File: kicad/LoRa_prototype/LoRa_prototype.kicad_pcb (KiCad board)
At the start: 4 copper layers, 138 parts, among them J1 Conn_ST_STDC14, J10 SYS, J11 BME, J12 GPS, J13 GPS_UART, J14 SPI_FLASH, J15 SYS, J18 MCO, J2 USB_C_Receptacle_PowerOnly_6P, J3 BAT, J4 SMA Female, J5 FG, J6 I2C1, J8 BMV, J9 UART1, Q1 DTC143Z, Q2 DTC143Z, SW1 NRST, U1 TC1262-33, U10 STM32WL54CCUx, U2 BQ24074RGTT, U3 MAX17048, U4 SPV1050, U5 AS179-92LF, U6 L80-R, U7 BME688, U8 W25Q16JVSS, U9 BMV080, X1 LSE, X2 NT2016SF

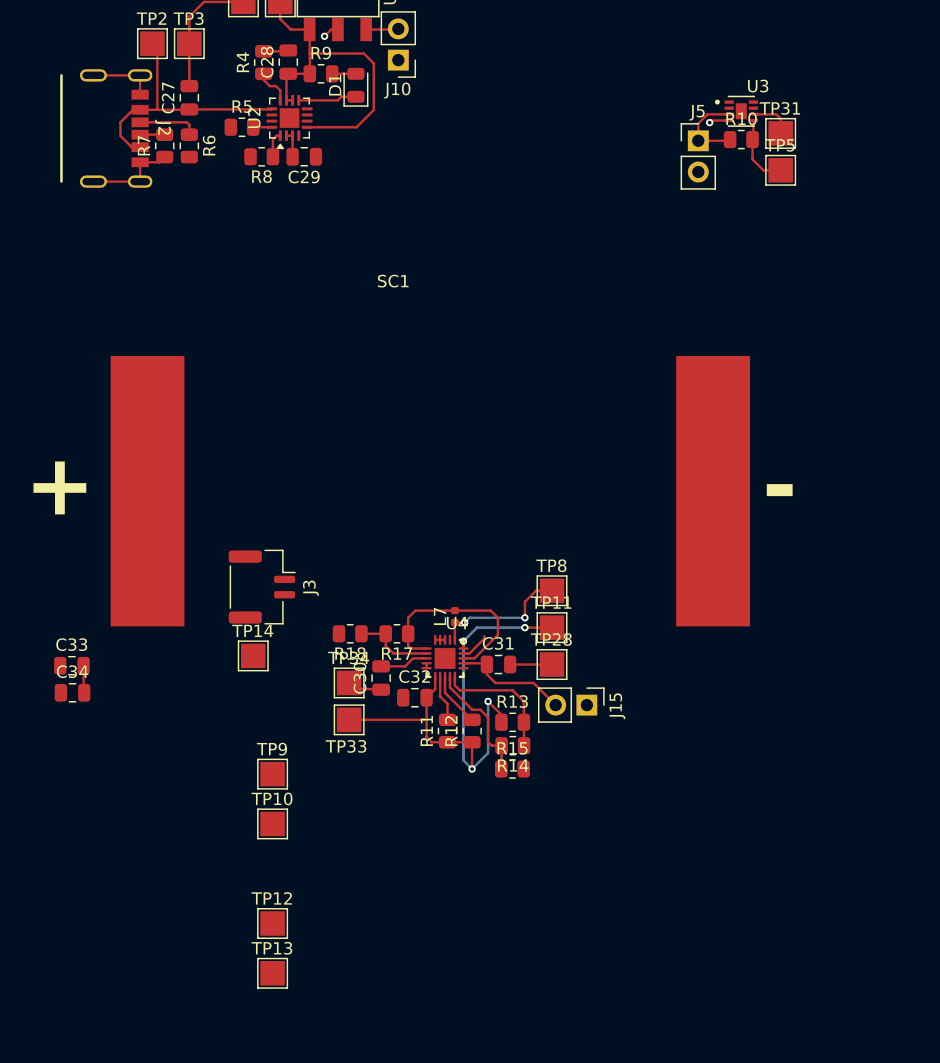
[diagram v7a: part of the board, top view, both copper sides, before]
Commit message: Done routing power sheet
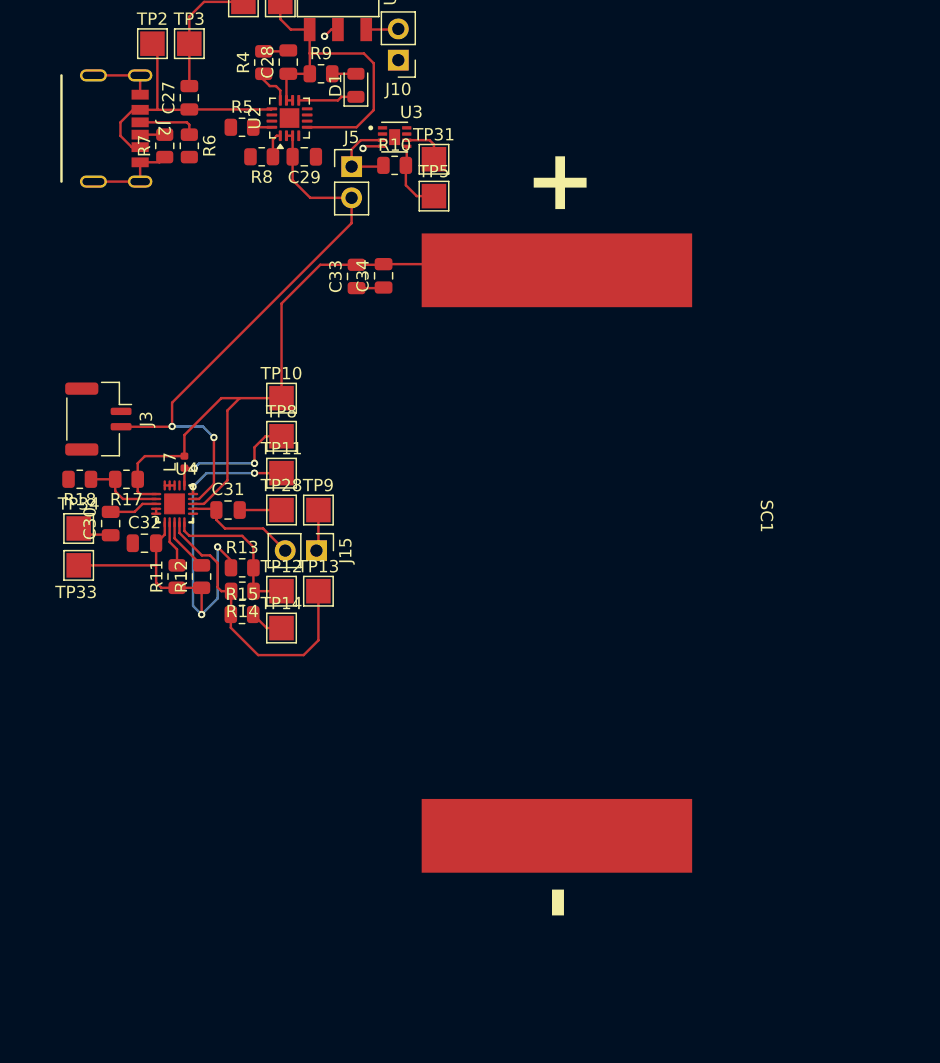
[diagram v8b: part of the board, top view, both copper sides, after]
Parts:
- moved C34 42.3 mm to (51.4, 55.9), turned to 90 degrees
- moved C33 39.2 mm to (49.2, 55.9), turned to 90 degrees
- moved TP10 34.6 mm to (43.1, 65.8)
- moved TP13 31.3 mm to (46.1, 81.5)
- moved J5 28.3 mm to (48.8, 47.0)
- moved R10 28.3 mm to (52.3, 46.9)
- moved TP31 28.3 mm to (55.5, 46.4)
- moved TP5 28.3 mm to (55.5, 49.4)
- moved U3 28.3 mm to (52.3, 44.6)
- moved TP12 27.0 mm to (43.1, 81.5)
- moved C30 25.3 mm to (29.2, 76.0)
- moved C31 25.3 mm to (38.8, 74.9)
- moved C32 25.3 mm to (31.9, 77.6)
- moved J15 25.3 mm to (45.9, 78.2)
- moved L7 25.3 mm to (35.2, 71.0)
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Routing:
- net /POWER/BAT+: track 4.60 -> 48.1 mm, vias 0 -> 2
- net /POWER/MPP: track 18.9 -> 61.1 mm
- net Net-(U4-EOC): track 10.1 -> 23.7 mm
- net GND: track 41.3 -> 46.2 mm
- net VDD: track 0.00 -> 3.37 mm
- net Net-(U4-UVP): track 10.4 -> 12.7 mm
